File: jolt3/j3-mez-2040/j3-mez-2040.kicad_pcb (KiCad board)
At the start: 4 copper layers, 38 x 38 mm, 35 parts, among them J29 USB_C_Receptacle_USB2.0_14P, J30 Conn_ARM_JTAG_SWD_10, SW1 SW_SPST, SW2 SW_SPST, U1 RP2040, U2 AP2112-M3.3, U3 W25Q128JVP, Y1 ABM8-272-T3

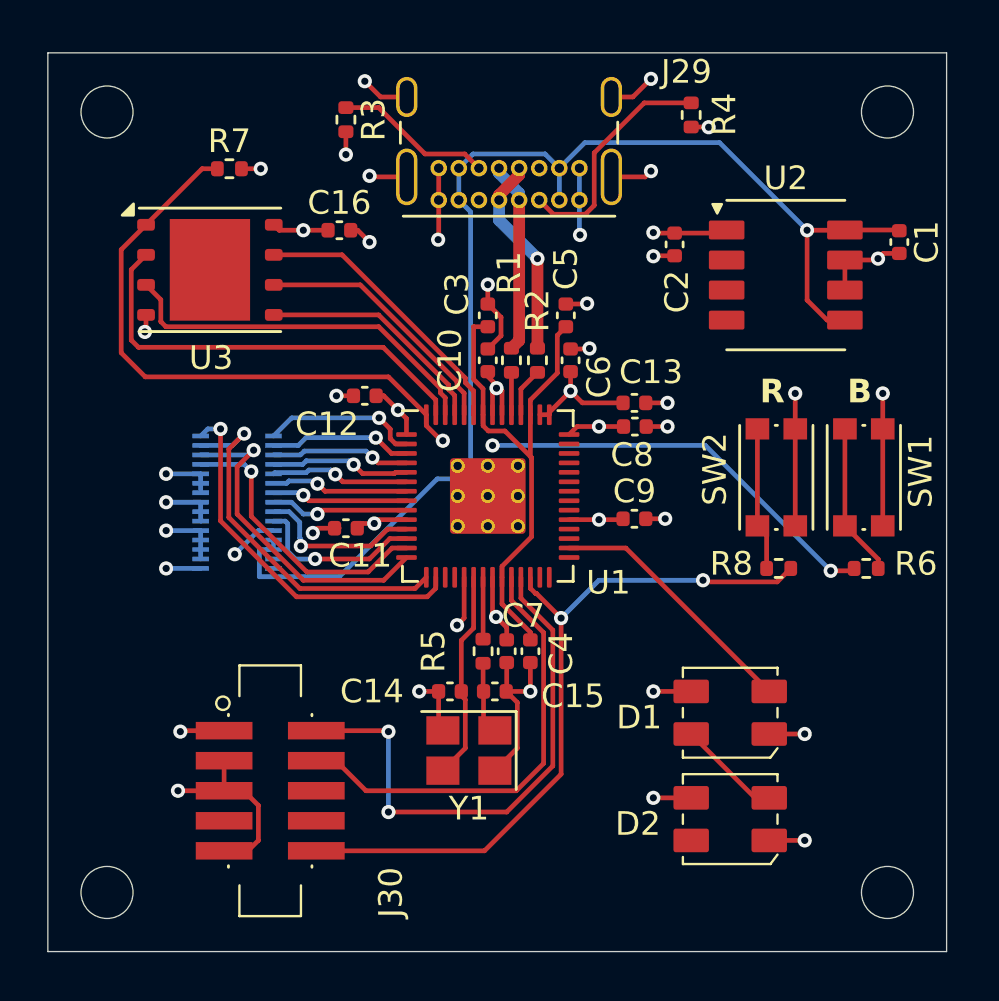
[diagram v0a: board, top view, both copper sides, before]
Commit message: Jolt 3: Rev A for 3 boards
Send Rev A out for jolt3-left, jolt3-right, and j3-mez-2040.
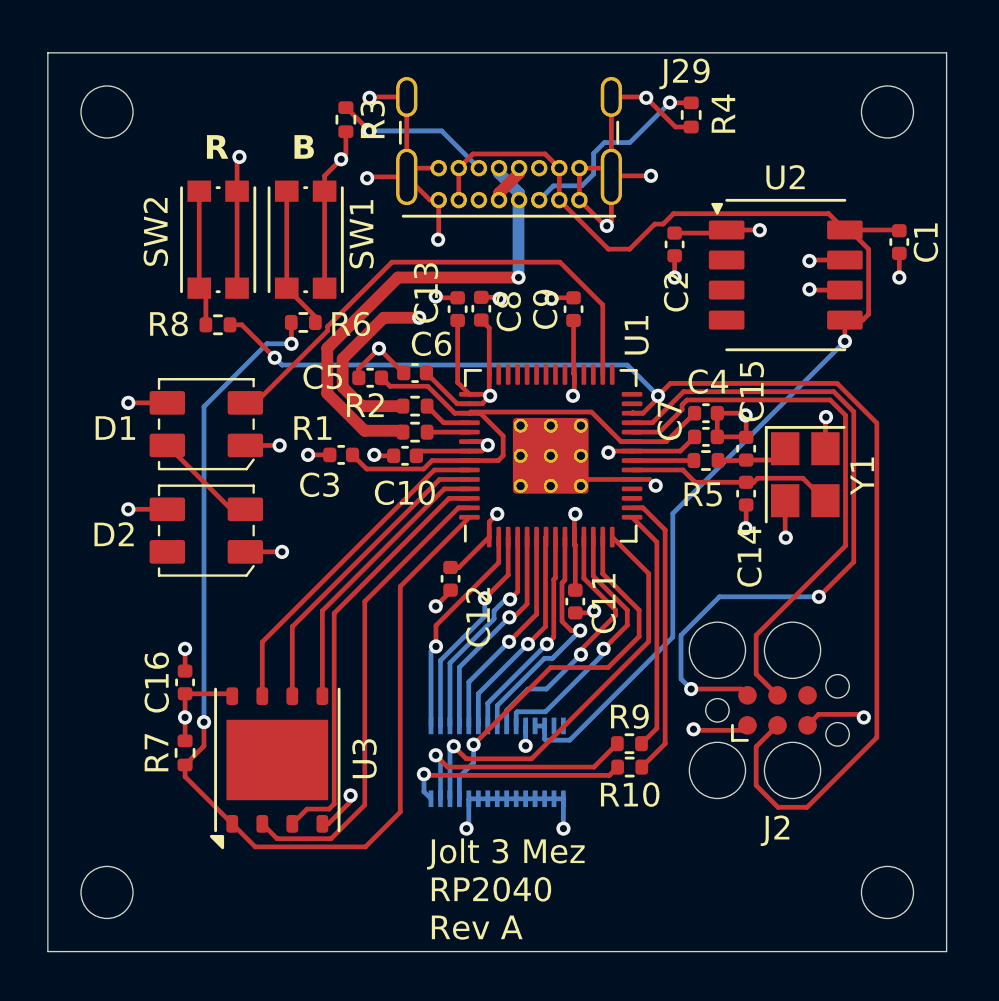
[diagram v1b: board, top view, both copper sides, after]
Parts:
- removed J30: Conn_ARM_JTAG_SWD_10, davidb-keyboard-foot:Cortex-M-Debug10
- added J2: Conn_ARM_SWD_TagConnect_TC2030, Connector:Tag-Connect_TC2030-IDC-FP_2x03_P1.27mm_Vertical, F.Cu at (130.3, 101.8)
- added R10: 27, Resistor_SMD:R_0402_1005Metric, F.Cu at (124.1, 104.2)
- added R9: 27, Resistor_SMD:R_0402_1005Metric, F.Cu at (124.1, 103.2)
- moved R6 26.0 mm to (110.3, 85.4)
- moved R8 25.9 mm to (106.7, 85.5)
- moved SW2 25.7 mm to (106.7, 81.9)
- moved SW1 25.7 mm to (110.4, 81.9)
- moved D1 25.3 mm to (106.2, 89.7)
- moved D2 25.3 mm to (106.2, 94.2)
- moved R7 24.8 mm to (105.3, 103.6), turned to 90 degrees
- moved U3 20.9 mm to (109.2, 103.9), turned to 90 degrees
- moved C16 20.2 mm to (105.3, 100.6), turned to 90 degrees
- moved Y1 18.4 mm to (131.5, 91.8), turned to -90 degrees
- moved J1 15.6 mm to (118.5, 104.0), turned to 90 degrees
- moved C14 15.1 mm to (129.0, 92.6), turned to 90 degrees
- moved C15 14.8 mm to (129.0, 90.7), turned to -90 degrees
- moved C4 12.5 mm to (127.3, 89.2), turned to 0 degrees
- moved R5 12.4 mm to (127.3, 91.2), turned to 180 degrees
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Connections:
- U1 pad 15: /MCU/SERTX -> Net-(U1-GPIO12)
- U1 pad 16: /MCU/SERRX -> Net-(U1-GPIO13)
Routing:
- net RUN: track 31.2 -> 53.9 mm
- net Net-(U1-GPIO13): track 0.00 -> 12.2 mm
- net /USB_D+: track 8.10 -> 20.1 mm, vias 0 -> 1
- net RGB: track 11.0 -> 21.4 mm
- net Net-(U1-GPIO12): track 0.00 -> 10.3 mm
- net GND: track 73.8 -> 83.2 mm
- net +3.3V: track 34.1 -> 42.9 mm, vias 14 -> 12
- net /USB_D-: track 8.64 -> 16.8 mm
- net SWDIO: track 22.8 -> 30.1 mm
- net /MCU/SERRX: track 15.9 -> 9.52 mm
- net /MCU/SERTX: track 15.7 -> 10.2 mm
- net SWCLK: track 19.0 -> 23.8 mm
- net /MCU/COL-B: track 5.90 -> 10.2 mm
- net /MCU/SDA: track 12.1 -> 16.3 mm
- net /MCU/COL-D: track 7.34 -> 11.2 mm
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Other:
- board text added: "Jolt 3 Mez RP2040 Rev A"
